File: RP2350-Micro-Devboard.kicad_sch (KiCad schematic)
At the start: 31 parts, among them J1 USB_C_Receptacle_USB2.0_14P, J2 Conn_01x07, J3 Conn_01x07, SW2 SW_Push, U1 MCP1700x-330xxTT, U2 RP2350_60QFN, Y1 12MHz

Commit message: first completion of shitty routing
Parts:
- removed J1: USB_C_Receptacle_USB2.0_14P, Connector_USB:USB_C_Receptacle_HRO_TYPE-C-31-M-12, symbol Connector:USB_C_Receptacle_USB2.0_14P
- removed R1, R2: 5.1k, Resistor_SMD:R_0402_1005Metric, symbol Device:R
- added J4: USB_B_Micro, RP2350_60QFN_minimal:USB_Micro-B_Amphenol_10103594-0001LF_Horizontal_modified, symbol Connector:USB_B_Micro
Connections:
- net GND: now also J4.5 (GND), J4.6 (Shield)
- net GPIO0: now also J2.1 (Pin_1); no longer J2.7 (Pin_7)
- net GPIO1: now also J2.2 (Pin_2); no longer J3.1 (Pin_1)
- net GPIO2: now also J2.3 (Pin_3); no longer J3.2 (Pin_2)
- net GPIO26: now also J3.2 (Pin_2); no longer J2.1 (Pin_1)
- net GPIO27: now also J3.3 (Pin_3); no longer J2.2 (Pin_2)
- net GPIO28: now also J3.4 (Pin_4); no longer J2.3 (Pin_3)
- net GPIO3: now also J2.4 (Pin_4); no longer J3.4 (Pin_4)
- net GPIO4: now also J2.5 (Pin_5); no longer J3.3 (Pin_3)
- net GPIO5: now also J2.6 (Pin_6); no longer J2.4 (Pin_4)
- net GPIO6: now also J2.7 (Pin_7); no longer J2.5 (Pin_5)
- net GPIO7: now also J3.1 (Pin_1); no longer J2.6 (Pin_6)
- net USB_D+: now also J4.3 (D+)
- net USB_D-: now also J4.2 (D-)
- net VBUS: now also J4.1 (VBUS)
- no-connect marks 27 -> 28
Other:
- moved on the sheet: C11, C12, U1

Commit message: fix and make consistent values
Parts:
- C1, C10, C2, C3, C4, C5, C6, C7, C8: value 100n -> 0.1uF
- C11, C12: value 10u -> 10uF
- C9: value 4.7u -> 4.7uF
- R3, R4: value 27 -> 27Ω
- R5: value 1k -> 1kΩ
- R8: value 33 -> 33Ω
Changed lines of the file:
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@@
 			)
 		)
-		(property "Value" "10u"
+		(property "Value" "10uF"
 			(at 82.55 38.0999 0)
 			(effects
@@
 			)
 		)
-		(property "Value" "100n"
+		(property "Value" "0.1uF"
 			(at 158.75 29.2099 0)
 			(effects
@@
 			)
 		)
-		(property "Value" "100n"
+		(property "Value" "0.1uF"
 			(at 193.04 29.2099 0)
 			(effects
@@
 			)
 		)
-		(property "Value" "100n"
+		(property "Value" "0.1uF"
 			(at 227.33 29.2099 0)
 			(effects
@@
 			)
 		)
-		(property "Value" "1k"
+		(property "Value" "1kΩ"
 			(at 276.86 35.5599 0)
 			(effects
@@
 			)
 		)
-		(property "Value" "100n"
+		(property "Value" "0.1uF"
 			(at 123.19 29.2099 0)
 			(effects
@@
 			)
 		)
-		(property "Value" "27"
+		(property "Value" "27Ω"
 			(at 227.33 55.8799 0)
 			(effects
@@
 			)
 		)
-		(property "Value" "27"
+		(property "Value" "27Ω"
 			(at 234.95 55.8799 0)
 			(effects
@@
 			)
 		)
-		(property "Value" "4.7u"
+		(property "Value" "4.7uF"
 			(at 134.62 29.2099 0)
 			(effects
@@
 			)
 		)
-		(property "Value" "100n"
+		(property "Value" "0.1uF"
 			(at 204.47 29.2099 0)
 			(effects
@@
 			)
 		)
-		(property "Value" "100n"
+		(property "Value" "0.1uF"
 			(at 181.61 29.2099 0)
 			(effects
@@
 			)
 		)
-		(property "Value" "100n"
+		(property "Value" "0.1uF"
 			(at 215.9 29.2099 0)
 			(effects
@@
 			)
 		)
-		(property "Value" "10u"
+		(property "Value" "10uF"
 			(at 58.42 38.0999 0)
 			(effects
@@
 			)
 		)
-		(property "Value" "33"
+		(property "Value" "33Ω"
 			(at 134.62 49.53 90)
 			(effects
@@
 			)
 		)
-		(property "Value" "100n"
+		(property "Value" "0.1uF"
 			(at 170.18 29.2099 0)
 			(effects
@@
 			)
 		)
-		(property "Value" "100n"
+		(property "Value" "0.1uF"
 			(at 146.05 29.2099 0)
 			(effects

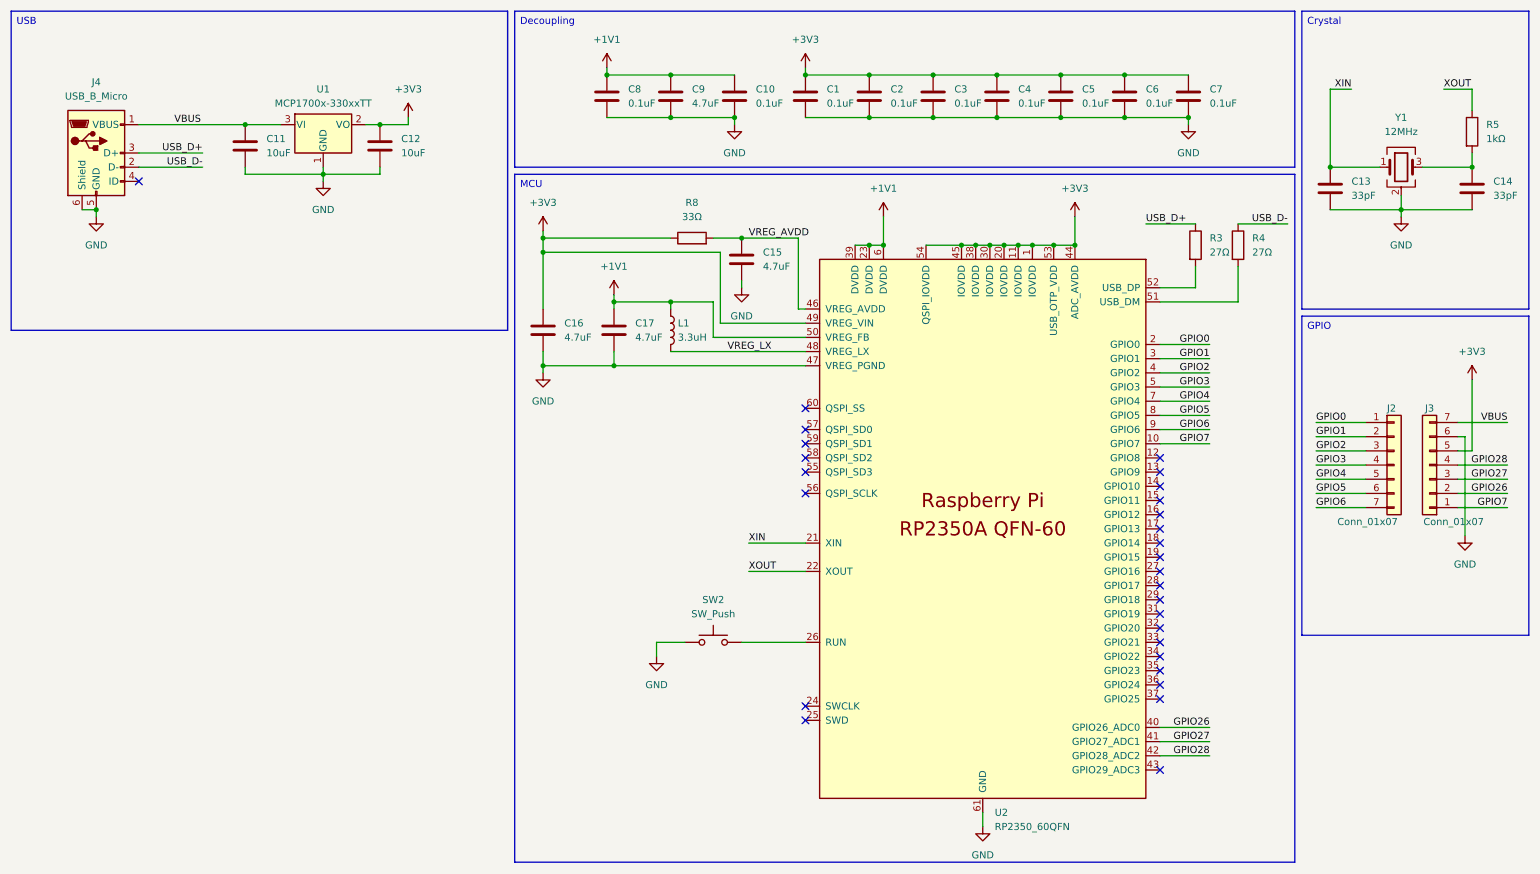
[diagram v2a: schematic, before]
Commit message: add testpoints, add buttons
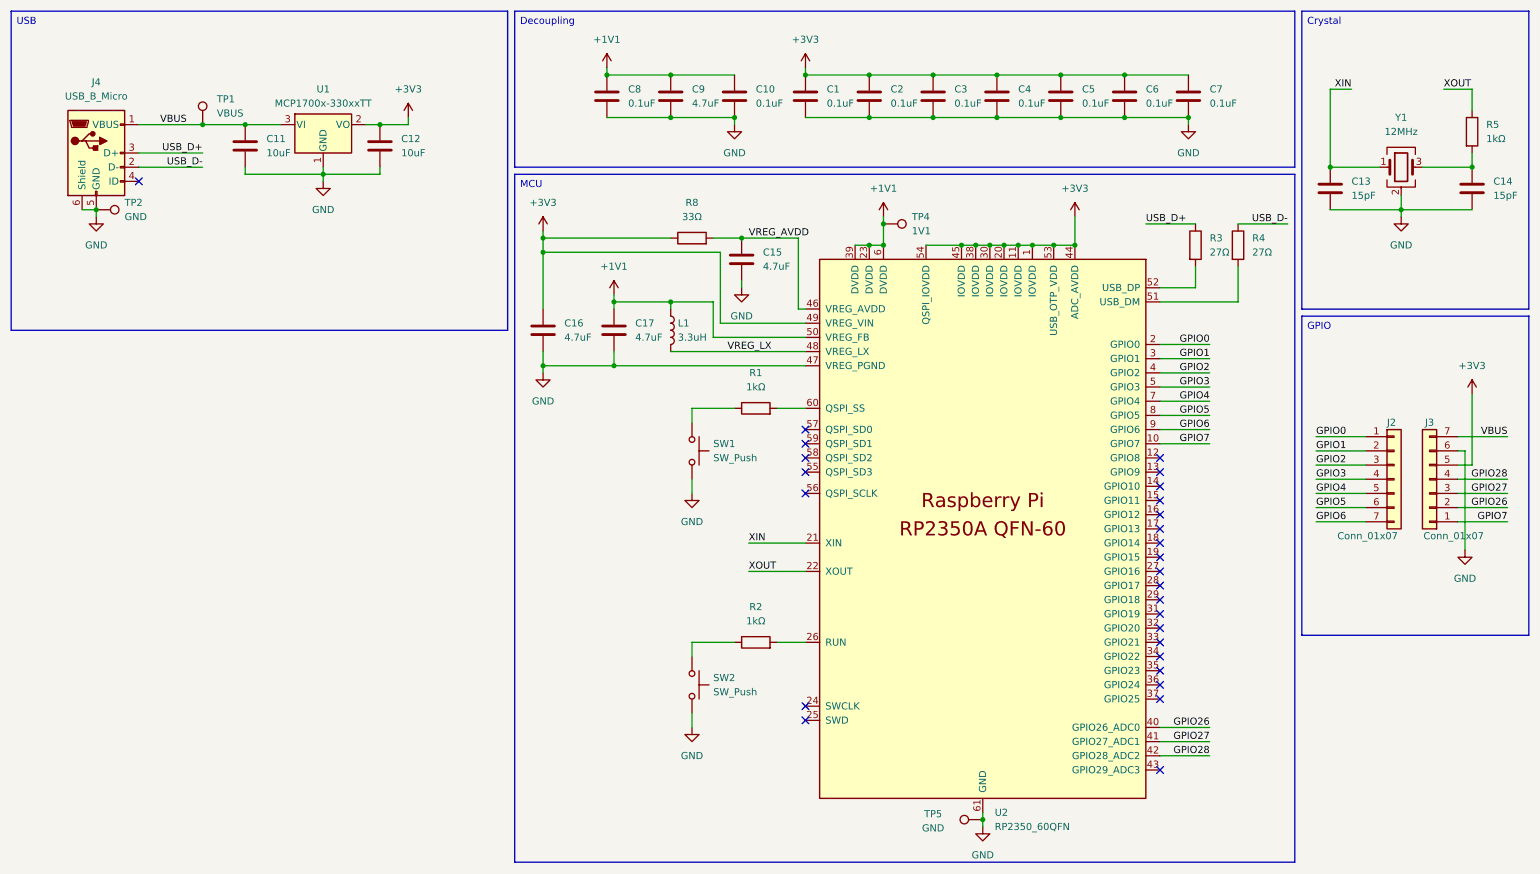
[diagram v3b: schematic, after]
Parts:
- added R1, R2: 1kΩ, Resistor_SMD:R_0402_1005Metric, symbol Device:R
- added SW1: SW_Push, Button_Switch_SMD:SW_Push_SPST_NO_Alps_SKRK, symbol Switch:SW_Push
- added TP1: VBUS, TestPoint:TestPoint_Pad_D1.0mm, symbol Connector:TestPoint
- added TP2, TP5: GND, TestPoint:TestPoint_Pad_D1.0mm, symbol Connector:TestPoint
- added TP4: 1V1, TestPoint:TestPoint_Pad_D1.0mm, symbol Connector:TestPoint
- C13, C14: value 33pF -> 15pF
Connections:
- net +1V1: now also TP4.1
- net GND: now also SW2.2, SW1.2, TP2.1, TP5.1; no longer SW2.1
- net VBUS: now also TP1.1
- net at U2.26 (RUN): now also R2.2; no longer SW2.2
- net at U2.60 (QSPI_SS): now also R1.2
- new net: R1.1, SW1.1
- new net: R2.1, SW2.1
- no-connect marks 28 -> 27
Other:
- moved on the sheet: J2, J3, SW2
